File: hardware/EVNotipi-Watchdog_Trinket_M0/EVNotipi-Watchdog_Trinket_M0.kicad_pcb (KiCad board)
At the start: 2 copper layers, 25 x 34 mm, 11 parts, among them J1 Conn_Left, J2 Conn_Right, J3 Conn_Pi, J4 Conn_Pwr, J5 Conn_01x04_Male, Q1 BS170, Q2 IRF5305, U1 TSR_2-2450

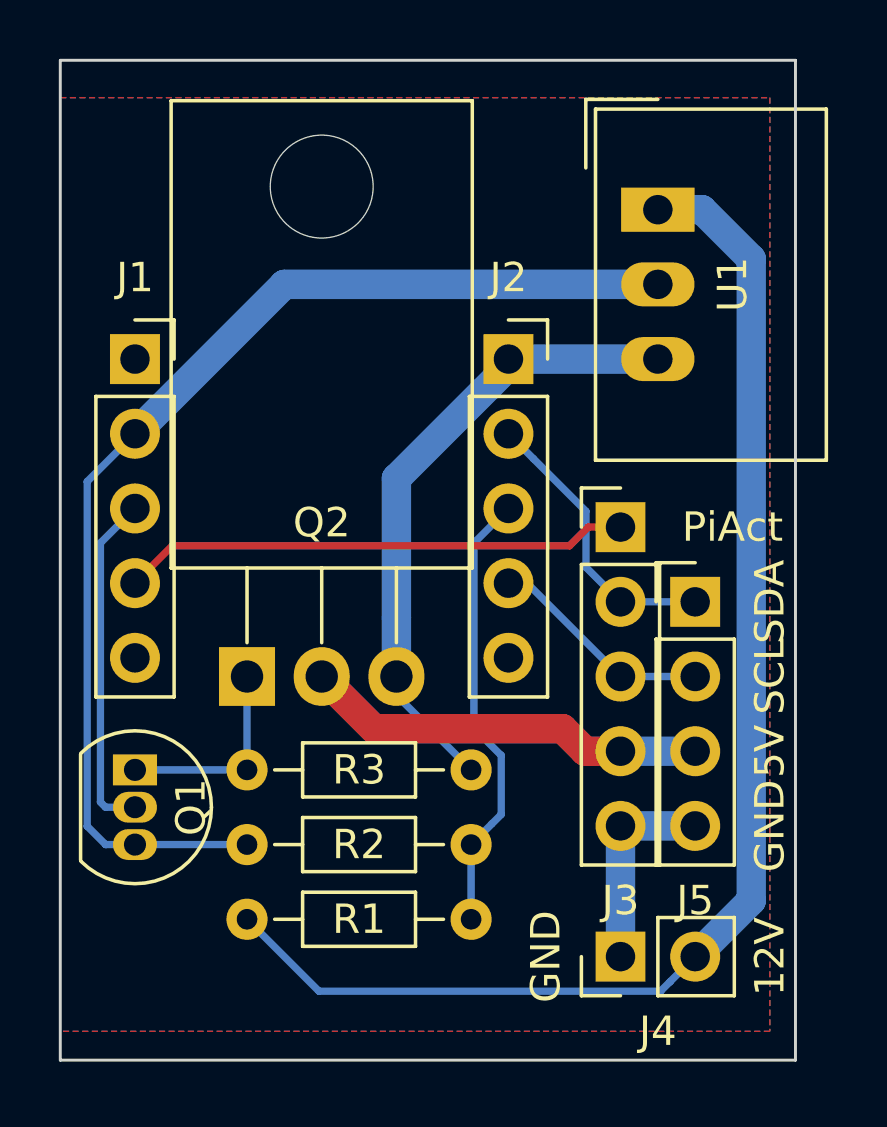
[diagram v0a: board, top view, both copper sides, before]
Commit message: Add buffer capacitor and a diode for backflow suppression and protection from polarity reversal
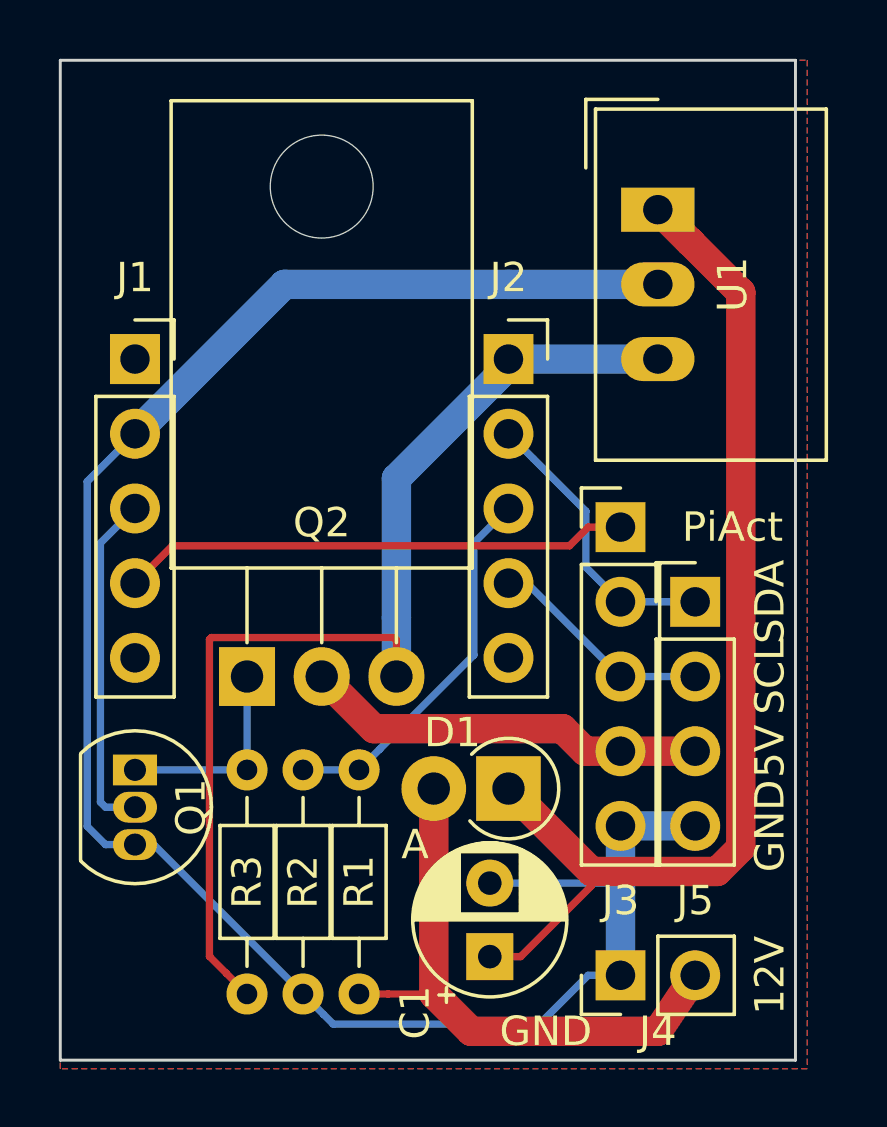
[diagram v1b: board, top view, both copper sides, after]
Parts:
- added C1: CP, Capacitor_THT:CP_Radial_D5.0mm_P2.50mm, F.Cu at (69.2, 61.0)
- added D1: D_Schottky, Diode_THT:D_DO-41_SOD81_P2.54mm_Vertical_AnodeUp, F.Cu at (69.8, 55.2)
- J1: value Conn_Left -> Conn_M0_Left
- J2: value Conn_Right -> Conn_M0_Right
- J5: value Conn_01x04_Male -> Conn_i2c
- moved R2 5.43 mm to (62.9, 62.2), turned to 90 degrees
- moved R1 4.58 mm to (64.8, 62.2), turned to 90 degrees
- moved J4 0.63 mm to (73.7, 61.6)
- turned R3 to 270 degrees
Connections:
- U1 pad 1: VCC12V -> Net-(C1-Pad1)
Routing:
- net Net-(C1-Pad1): track 0.00 -> 37.7 mm
- net VCC12V: track 45.1 -> 20.0 mm
- net GND: track 46.6 -> 67.5 mm
- net VCC5V: track 21.7 -> 37.7 mm
- net ADC: track 15.3 -> 12.9 mm
